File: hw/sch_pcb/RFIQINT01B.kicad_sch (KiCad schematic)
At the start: 48 parts, among them J1 HEADER_2x04_PARALLEL, J2 SATA7-67491-1030, J3 HEADER_1x08, J4 SATA7-67491-1030, J5 HEADER_1x08, J6 SATA7-67491-1030, M1 HOLE, M2 HOLE, M3 HOLE, M4 HOLE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

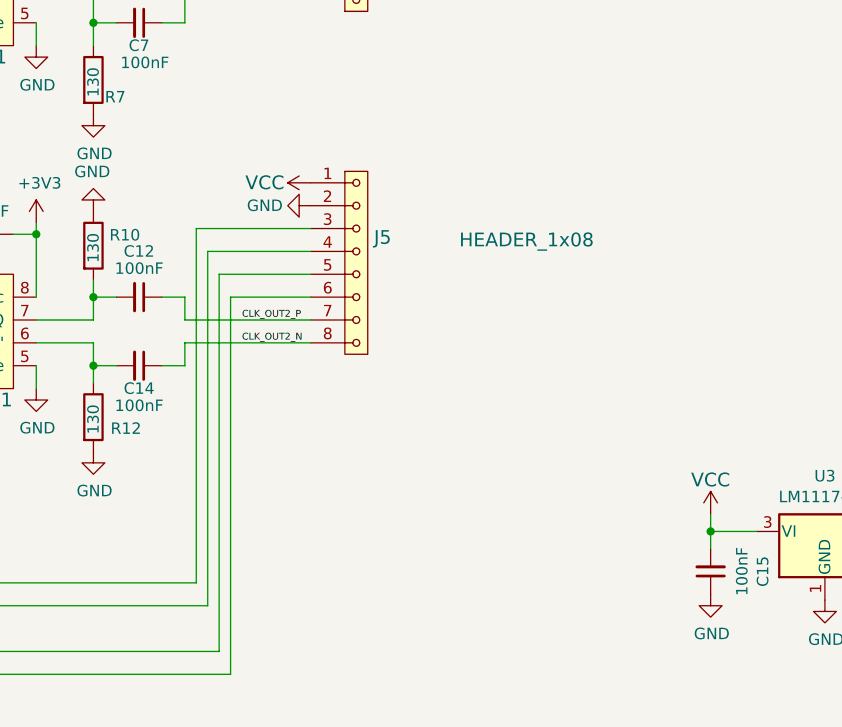
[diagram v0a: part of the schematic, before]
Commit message: Fix differential pair routing #3.
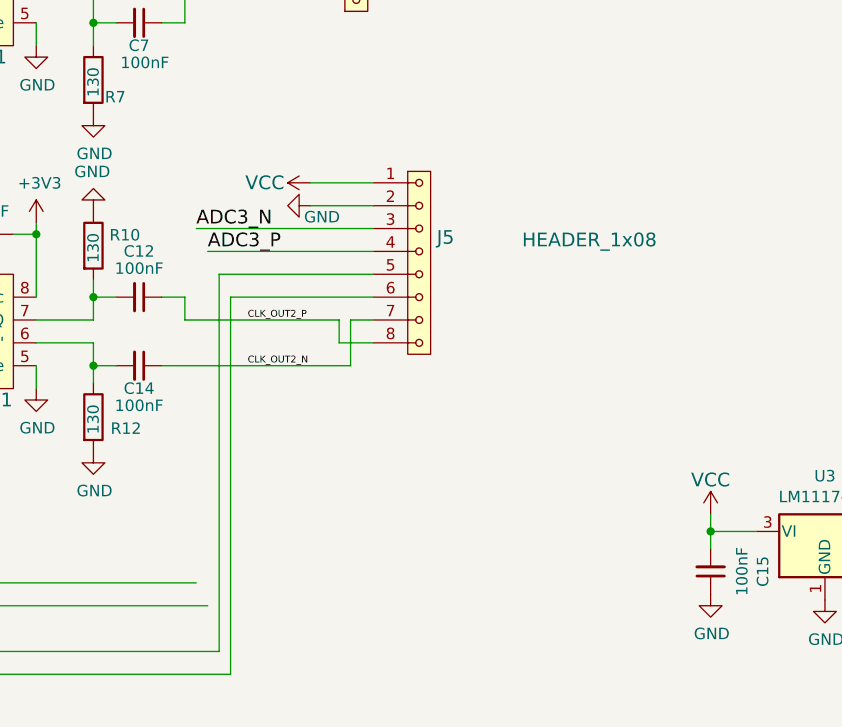
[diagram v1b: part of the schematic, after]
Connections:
- net ADC3_N: now also J5.3; no longer J5.4
- net ADC3_P: now also J5.4; no longer J5.3
- net CLK_OUT2_N: now also J5.7; no longer J5.8
- net CLK_OUT2_P: now also J5.8; no longer J5.7
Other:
- moved on the sheet: J5
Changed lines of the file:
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@@
+    (stroke (width 0) (type default) (color 0 0 0 0))
+  )
+  (wire (pts (xy 149.86 113.03) (xy 167.005 113.03))
     (stroke (width 0) (type default) (color 0 0 0 0))
   )
@@
     (stroke (width 0) (type default) (color 0 0 0 0))
   )
-  (wire (pts (xy 152.4 105.41) (xy 163.83 105.41))
+  (wire (pts (xy 152.4 105.41) (xy 170.815 105.41))
+    (stroke (width 0) (type default) (color 0 0 0 0))
+  )
+  (wire (pts (xy 170.815 100.33) (xy 163.83 100.33))
     (stroke (width 0) (type default) (color 0 0 0 0))
   )
@@
     (stroke (width 0) (type default) (color 0 0 0 0))
   )
-  (wire (pts (xy 151.13 102.87) (xy 163.83 102.87))
+  (wire (pts (xy 151.13 102.87) (xy 170.815 102.87))
     (stroke (width 0) (type default) (color 0 0 0 0))
   )
@@
     (stroke (width 0) (type default) (color 0 0 0 0))
   )
-  (wire (pts (xy 154.94 110.49) (xy 163.83 110.49))
+  (wire (pts (xy 154.94 110.49) (xy 170.815 110.49))
     (stroke (width 0) (type default) (color 0 0 0 0))
   )
@@
     (stroke (width 0) (type default) (color 0 0 0 0))
   )
+  (wire (pts (xy 170.815 113.03) (xy 168.275 113.03))
+    (stroke (width 0) (type default) (color 0 0 0 0))
+  )
   (polyline (pts (xy 278.13 44.45) (xy 278.13 54.61))
     (stroke (width 0) (type default) (color 0 0 0 0))
@@
     (stroke (width 0) (type default) (color 0 0 0 0))
   )
+  (wire (pts (xy 167.005 115.57) (xy 167.005 113.03))
+    (stroke (width 0) (type default) (color 0 0 0 0))
+  )
   (wire (pts (xy 114.3 74.93) (xy 116.84 74.93))
     (stroke (width 0) (type default) (color 0 0 0 0))
@@
     (stroke (width 0) (type default) (color 0 0 0 0))
   )
+  (wire (pts (xy 170.815 97.79) (xy 163.83 97.79))
+    (stroke (width 0) (type default) (color 0 0 0 0))
+  )
   (wire (pts (xy 260.35 34.29) (xy 252.73 34.29))
     (stroke (width 0) (type default) (color 0 0 0 0))
@@
     (stroke (width 0) (type default) (color 0 0 0 0))
   )
-  (wire (pts (xy 147.32 118.11) (xy 149.86 118.11))
+  (wire (pts (xy 147.32 118.11) (xy 168.275 118.11))
     (stroke (width 0) (type default) (color 0 0 0 0))
   )
@@
     (stroke (width 0) (type default) (color 0 0 0 0))
   )
-  (wire (pts (xy 149.86 115.57) (xy 163.83 115.57))
-    (stroke (width 0) (type default) (color 0 0 0 0))
-  )
   (wire (pts (xy 114.3 118.11) (xy 114.3 115.57))
     (stroke (width 0) (type default) (color 0 0 0 0))
@@
     (stroke (width 0) (type default) (color 0 0 0 0))
   )
+  (wire (pts (xy 168.275 113.03) (xy 168.275 118.11))
+    (stroke (width 0) (type default) (color 0 0 0 0))
+  )
   (wire (pts (xy 252.73 34.29) (xy 245.11 34.29))
     (stroke (width 0) (type default) (color 0 0 0 0))
@@
     (stroke (width 0) (type default) (color 0 0 0 0))
   )
+  (wire (pts (xy 167.005 115.57) (xy 170.815 115.57))
+    (stroke (width 0) (type default) (color 0 0 0 0))
+  )
   (wire (pts (xy 152.4 69.85) (xy 152.4 43.18))
     (stroke (width 0) (type default) (color 0 0 0 0))
@@
     (stroke (width 0) (type default) (color 0 0 0 0))
   )
-  (wire (pts (xy 151.13 142.24) (xy 151.13 102.87))
-    (stroke (width 0) (type default) (color 0 0 0 0))
-  )
   (wire (pts (xy 91.44 100.33) (xy 91.44 99.06))
     (stroke (width 0) (type default) (color 0 0 0 0))
@@
     (stroke (width 0) (type default) (color 0 0 0 0))
   )
-  (wire (pts (xy 149.86 113.03) (xy 163.83 113.03))
-    (stroke (width 0) (type default) (color 0 0 0 0))
-  )
   (wire (pts (xy 97.79 91.44) (xy 100.33 91.44))
     (stroke (width 0) (type default) (color 0 0 0 0))
@@
     (stroke (width 0) (type default) (color 0 0 0 0))
   )
-  (wire (pts (xy 149.86 118.11) (xy 149.86 115.57))
-    (stroke (width 0) (type default) (color 0 0 0 0))
-  )
   (wire (pts (xy 114.3 72.39) (xy 114.3 74.93))
     (stroke (width 0) (type default) (color 0 0 0 0))
@@
     (stroke (width 0) (type default) (color 0 0 0 0))
   )
-  (wire (pts (xy 153.67 107.95) (xy 163.83 107.95))
+  (wire (pts (xy 153.67 107.95) (xy 170.815 107.95))
     (stroke (width 0) (type default) (color 0 0 0 0))
   )
@@
   )
   (wire (pts (xy 97.79 91.44) (xy 91.44 91.44))
-    (stroke (width 0) (type default) (color 0 0 0 0))
-  )
-  (wire (pts (xy 152.4 144.78) (xy 152.4 105.41))
     (stroke (width 0) (type default) (color 0 0 0 0))
   )
@@
     (effects (font (size 0.762 0.762)) (justify left bottom))
   )
+  (label "ADC3_N" (at 151.13 102.87 0)
+    (effects (font (size 1.524 1.524)) (justify left bottom))
+  )
   (label "CLK_IN1_P" (at 85.09 72.39 0)
     (effects (font (size 0.762 0.762)) (justify left bottom))
   )
-  (label "CLK_OUT2_N" (at 156.21 115.57 0)
+  (label "CLK_OUT2_N" (at 156.845 118.11 0)
     (effects (font (size 0.762 0.762)) (justify left bottom))
+  )
+  (label "ADC3_P" (at 152.4 105.41 0)
+    (effects (font (size 1.524 1.524)) (justify left bottom))
   )
   (label "CLK_OUT1_P" (at 153.035 74.93 0)
@@
     (effects (font (size 0.762 0.762)) (justify left bottom))
   )
-  (label "CLK_OUT2_P" (at 156.21 113.03 0)
+  (label "CLK_OUT2_P" (at 156.845 113.03 0)
     (effects (font (size 0.762 0.762)) (justify left bottom))
   )
@@
       (effects (font (size 1.524 1.524)) (justify left) hide)
     )
-    (property "Datasheet" "" (id 3) (at 168.91 77.47 0)
-      (effects (font (size 1.524 1.524)))
+    (property "Datasheet" "https://www.tme.com/Document/4e9cf481f3d9b179aa09f3a743bc9b2b/IDC381-x-110_KRONE.pdf" (id 3) (at 168.91 77.47 0)
+      (effects (font (size 1.524 1.524)) hide)
     )
     (property "UST_ID" "5c70984712875079b91f8b89" (id 4) (at 168.91 68.58 0)
@@
     (pin "7")
   )
-  (symbol (lib_id "RFIQINT01A-rescue:HEADER_1x08-MLAB_HEADER") (at 168.91 106.68 0) (unit 1)
-    (in_bom yes) (on_board yes)
-    (property "Reference" "J5" (id 0) (at 170.8658 103.8606 0)
+  (symbol (lib_id "RFIQINT01A-rescue:HEADER_1x08-MLAB_HEADER") (at 175.895 106.68 0) (unit 1)
+    (in_bom yes) (on_board yes)
+    (property "Reference" "J5" (id 0) (at 177.8508 103.8606 0)
       (effects (font (size 1.524 1.524)) (justify left))
     )
-    (property "Value" "HEADER_1x08" (id 1) (at 180.34 104.14 0)
+    (property "Value" "HEADER_1x08" (id 1) (at 187.325 104.14 0)
       (effects (font (size 1.524 1.524)) (justify left))
     )
-    (property "Footprint" "Mlab_CON:IDC381-8-110" (id 2) (at 170.8658 109.2454 0)
+    (property "Footprint" "Mlab_CON:IDC381-8-110" (id 2) (at 177.8508 109.2454 0)
       (effects (font (size 1.524 1.524)) (justify left) hide)
     )
-    (property "Datasheet" "" (id 3) (at 168.91 97.79 0)
-      (effects (font (size 1.524 1.524)))
-    )
-    (property "UST_ID" "5c70984712875079b91f8b89" (id 4) (at 168.91 106.68 0)
+    (property "Datasheet" "https://www.tme.com/Document/4e9cf481f3d9b179aa09f3a743bc9b2b/IDC381-x-110_KRONE.pdf" (id 3) (at 175.895 97.79 0)
+      (effects (font (size 1.524 1.524)) hide)
+    )
+    (property "UST_ID" "5c70984712875079b91f8b89" (id 4) (at 175.895 106.68 0)
       (effects (font (size 1.27 1.27)) hide)
     )
@@
       (effects (font (size 1.27 1.27)) hide)
     )
-    (property "Value" "GND" (id 1) (at 158.75 100.33 90))
+    (property "Value" "GND" (id 1) (at 165.1 101.6 90))
     (property "Footprint" "" (id 2) (at 163.83 100.33 0)
       (effects (font (size 1.27 1.27)) hide)

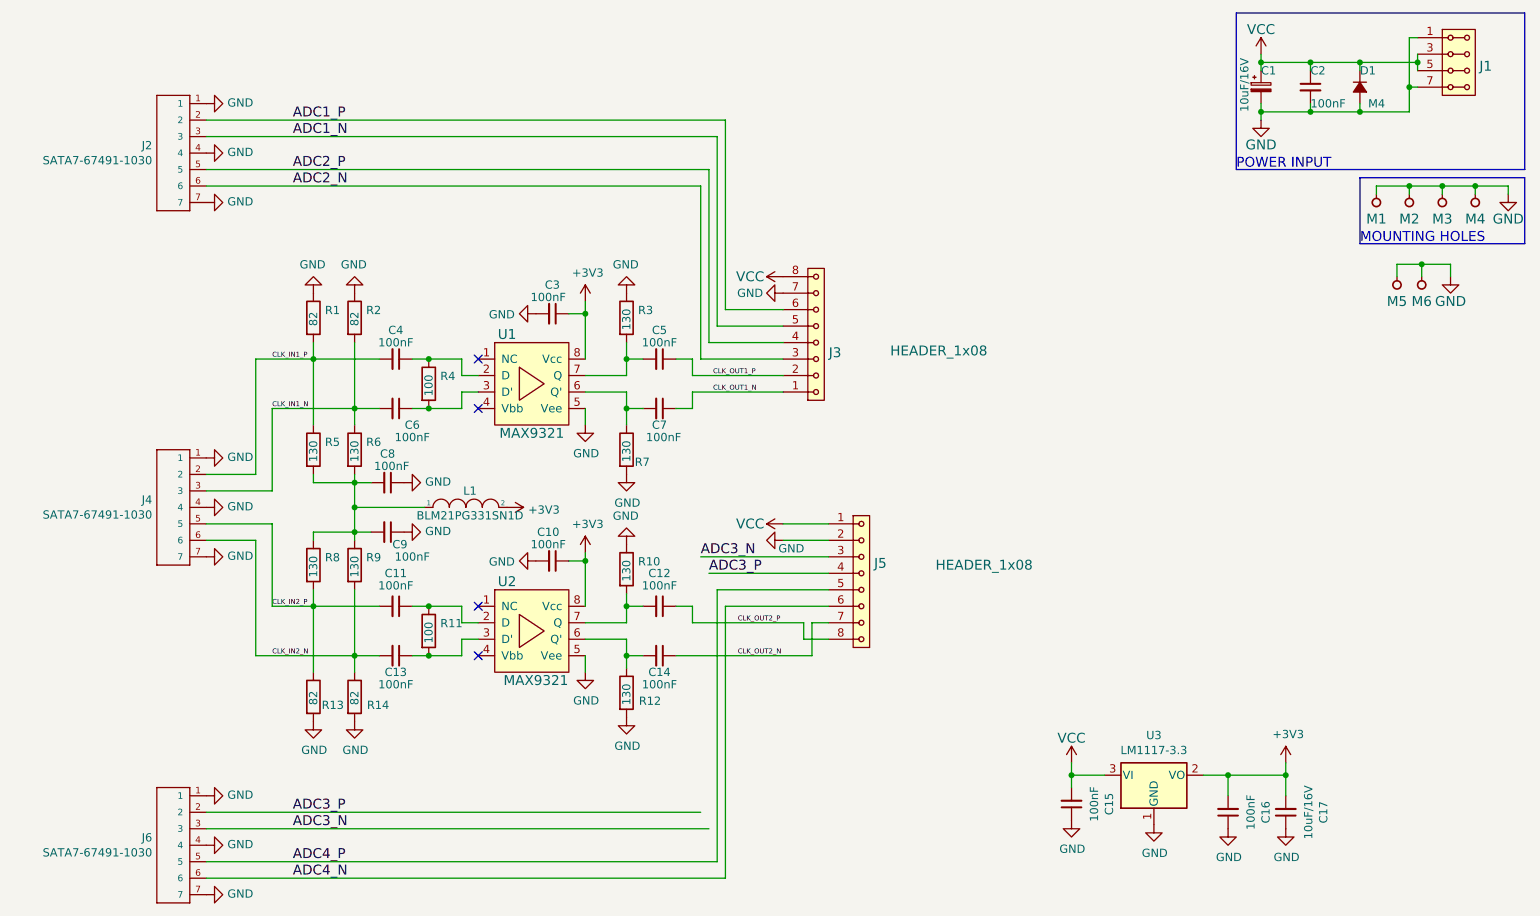
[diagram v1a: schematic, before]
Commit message: Editace podkladu pro osazovani
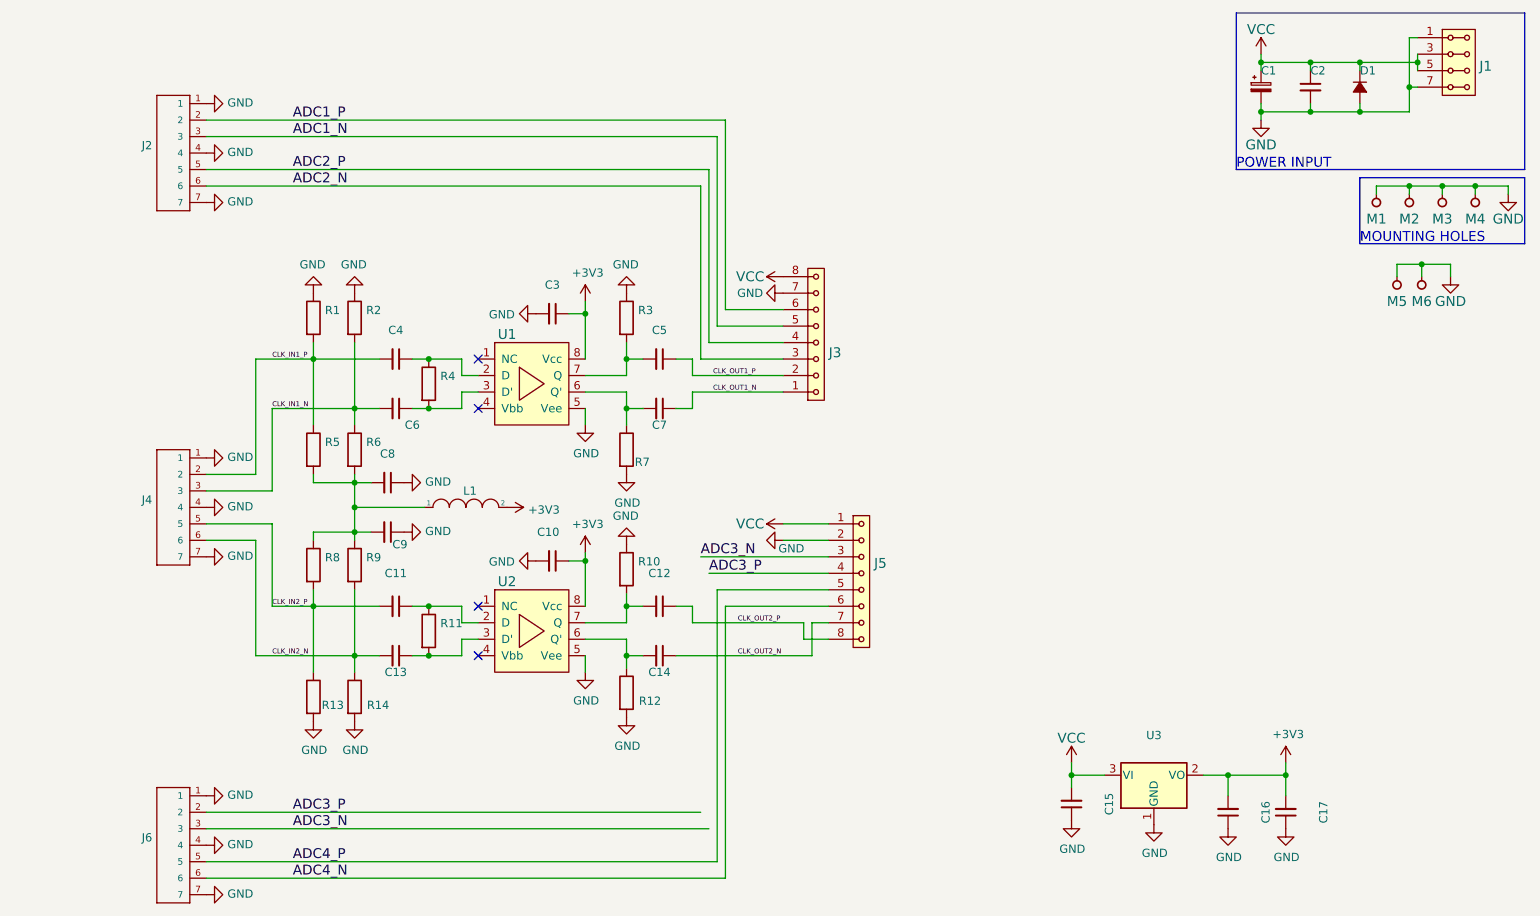
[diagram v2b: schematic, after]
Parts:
- C1, C17: value 10uF/16V -> (none); footprint Capacitor_SMD:C_0805_2012Metric -> (none)
- C10, C11, C12, C13, C14, C15, C16, C2, C3, C4, C5, C6, C7, C8, C9: value 100nF -> (none); footprint Capacitor_SMD:C_0603_1608Metric -> (none)
- D1: value M4 -> (none); footprint Diode_SMD:D_SMA -> (none)
- J1: value HEADER_2x04_PARALLEL -> (none); footprint Mlab_Pin_Headers:Straight_2x04 -> (none)
- J2, J4, J6: value SATA7-67491-1030 -> (none); footprint Mlab_CON:SATA-7_THT_VERT_2 -> (none)
- J3, J5: value HEADER_1x08 -> (none); footprint Mlab_CON:IDC381-8-110 -> (none)
- L1: value BLM21PG331SN1D -> (none); footprint Inductors_SMD:L_0805 -> (none)
- M1, M2, M3, M4, M5, M6: value HOLE -> (none); footprint Mlab_Mechanical:MountingHole_3mm -> (none)
- R1, R13, R14, R2: value 82 -> (none); footprint Resistor_SMD:R_0603_1608Metric -> (none)
- R10, R12, R3, R5, R6, R7, R8, R9: value 130 -> (none); footprint Resistor_SMD:R_0603_1608Metric -> (none)
- R11, R4: value 100 -> (none); footprint Resistor_SMD:R_0603_1608Metric -> (none)
- U1, U2: value MAX9321 -> (none); footprint Package_SO:SOIC-8_3.9x4.9mm_P1.27mm -> (none)
- U3: value LM1117-3.3 -> (none); footprint Package_TO_SOT_SMD:SOT-223-3_TabPin2 -> (none)
